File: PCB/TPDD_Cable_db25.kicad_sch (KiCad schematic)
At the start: 5 parts, among them J1 7 x wire pads, J2 DB25_Male, Q1 DTA114EKA, Q2 DTA114EKA, Q3 DTA114EKA

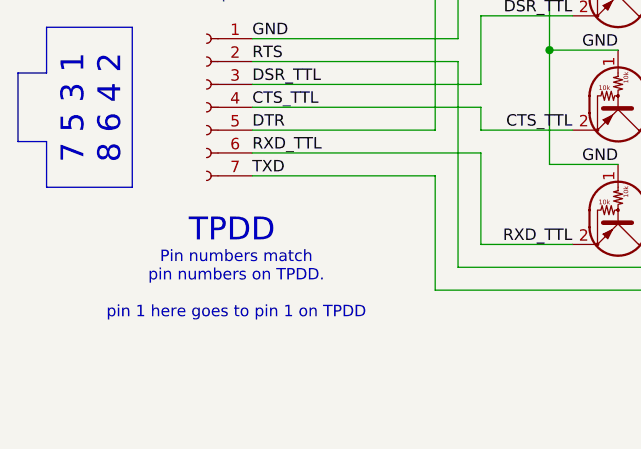
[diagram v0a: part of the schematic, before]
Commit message: schematics notes text
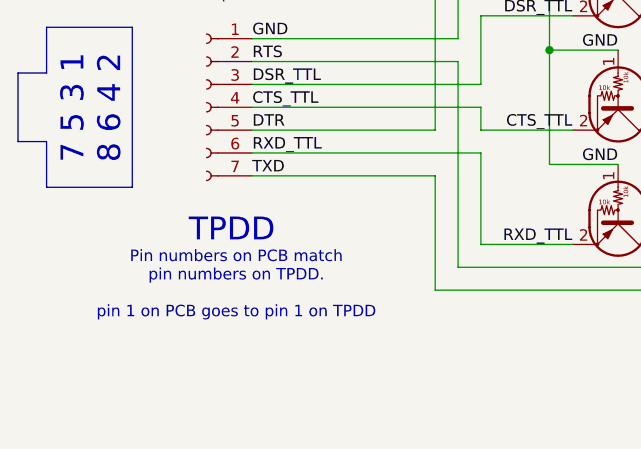
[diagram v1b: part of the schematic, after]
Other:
- note added: "Pin numbers on PCB match pin numbers on TPDD. pin 1 on PCB goes to pin 1 on TPDD"
- note removed: "Pin numbers match pin numbers on TPDD. pin 1 here goes to pin 1 on TPDD"
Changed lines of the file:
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@@
 		)
 	)
-	(text "Pin numbers match\npin numbers on TPDD.\n\npin 1 here goes to pin 1 on TPDD\n"
+	(text "Pin numbers on PCB match\npin numbers on TPDD.\n\npin 1 on PCB goes to pin 1 on TPDD\n"
 		(exclude_from_sim no)
 		(at 87.122 116.332 0)
